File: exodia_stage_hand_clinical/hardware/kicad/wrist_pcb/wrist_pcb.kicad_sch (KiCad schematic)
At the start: 9 parts, among them Q1 IRLZ44N, Q2 2N7002, Q3 2N7002, Q4 2N7002, Q5 2N7002, U1 ESP32S3_MODULE, U2 TP4056_IC

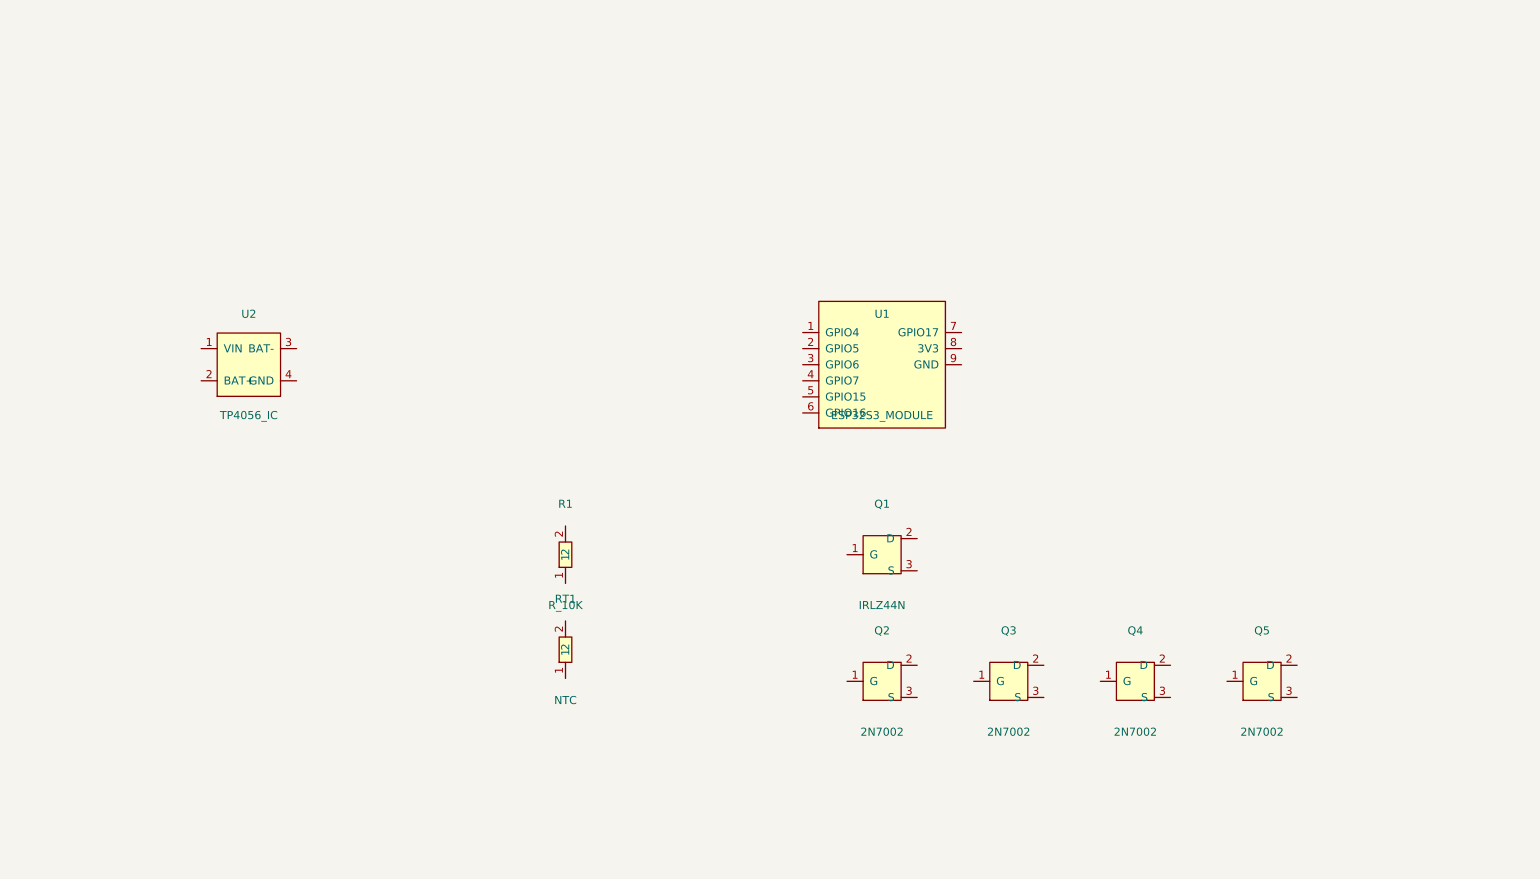
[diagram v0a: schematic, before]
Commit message: Auto-wire components using KiCad local labels and add ZIF/USB connectors
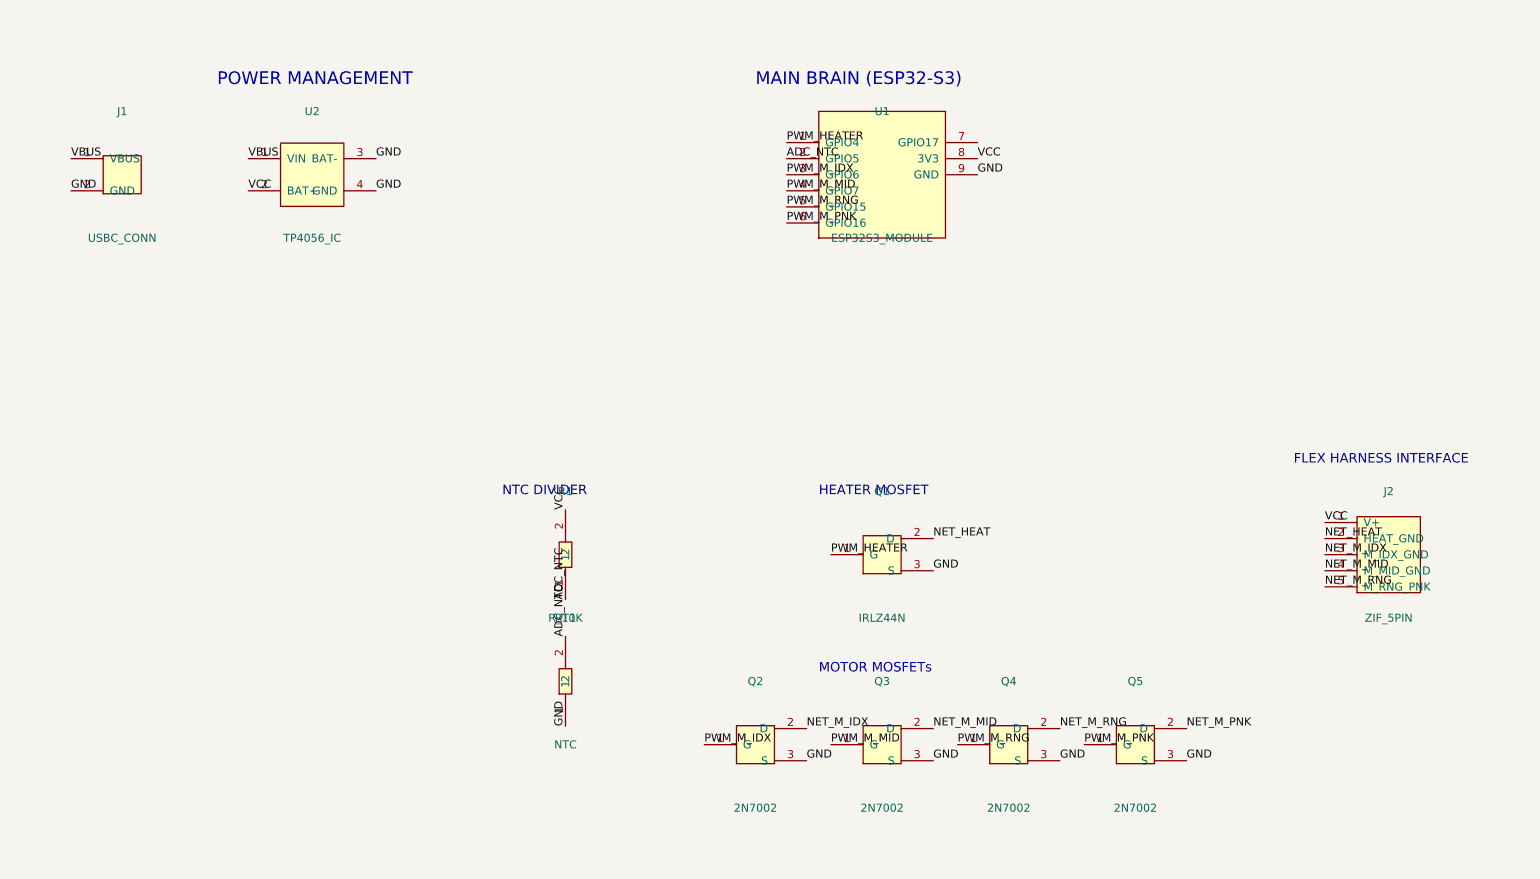
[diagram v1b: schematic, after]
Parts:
- added J1: USBC_CONN, symbol USBC_CONN
- added J2: ZIF_5PIN, symbol ZIF_5PIN
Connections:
- net VBUS: now reaches U2.1 (VIN)
- net VBUS: now also J1.1 (VBUS)
- net VCC: now reaches U2.2 (BAT+)
- net VCC: now also R1.2, U1.8 (3V3), J2.1 (V+)
- net GND: now reaches U2.3 (BAT-)
- net GND: now also Q1.3 (S), Q2.3 (S), Q3.3 (S), Q4.3 (S), Q5.3 (S), RT1.1, U1.9 (GND), U2.4 (GND), J1.2 (GND)
- net PWM_M_MID: now reaches Q3.1 (G)
- net PWM_M_MID: now also U1.4 (GPIO7)
- net NET_M_MID: now reaches Q3.2 (D)
- net NET_M_MID: now also J2.4 (M_MID_GND)
- net PWM_HEATER: now reaches Q1.1 (G)
- net PWM_HEATER: now also U1.1 (GPIO4)
- net NET_HEAT: now reaches Q1.2 (D)
- net NET_HEAT: now also J2.2 (HEAT_GND)
- net ADC_NTC: now reaches RT1.2
- net ADC_NTC: now also R1.1, U1.2 (GPIO5)
- net PWM_M_RNG: now reaches Q4.1 (G)
- net PWM_M_RNG: now also U1.5 (GPIO15)
- net NET_M_RNG: now reaches Q4.2 (D)
- net NET_M_RNG: now also J2.5 (M_RNG_PNK)
- net PWM_M_IDX: now reaches Q2.1 (G)
- net PWM_M_IDX: now also U1.3 (GPIO6)
- net NET_M_IDX: now reaches Q2.2 (D)
- net NET_M_IDX: now also J2.3 (M_IDX_GND)
- net PWM_M_PNK: now reaches Q5.1 (G)
- net PWM_M_PNK: now also U1.6 (GPIO16)
- net NET_M_PNK: now reaches Q5.2 (D)
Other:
- note added: "FLEX HARNESS INTERFACE"
- note added: "HEATER MOSFET"
- note added: "MAIN BRAIN (ESP32-S3)"
- note added: "MOTOR MOSFETs"
- note added: "NTC DIVIDER"
- note added: "POWER MANAGEMENT"

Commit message: Fix KiCad ERC errors (power flags, grid alignment, pin direction)
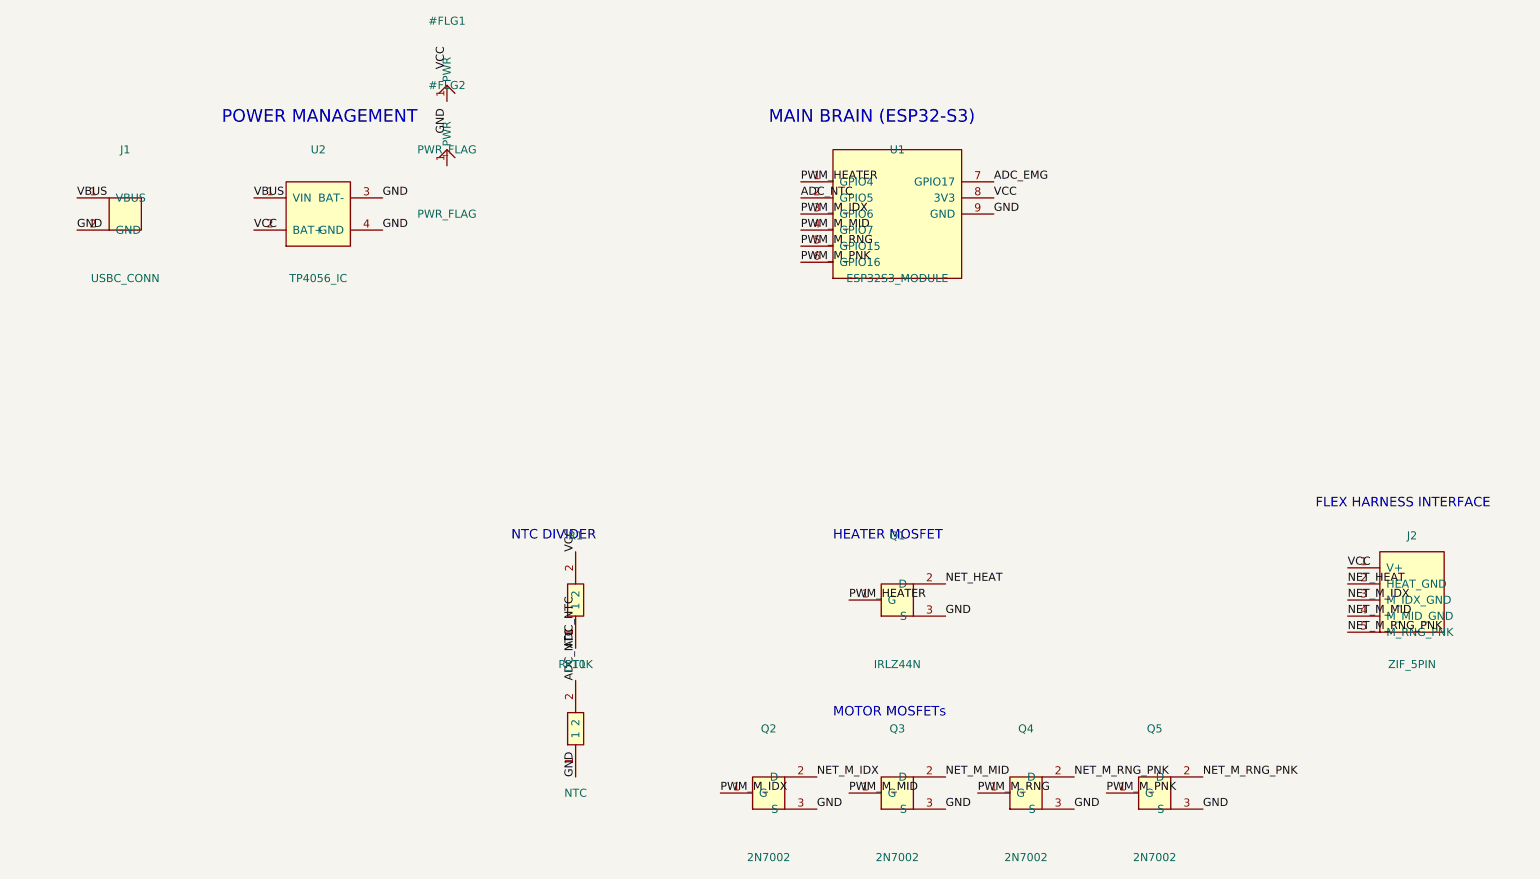
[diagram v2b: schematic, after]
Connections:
- net NET_M_RNG is gone; now on net NET_M_RNG_PNK: J2.5 (M_RNG_PNK), Q4.2 (D)
- net ADC_EMG: now reaches U1.7 (GPIO17)
- net NET_M_PNK renamed NET_M_RNG_PNK

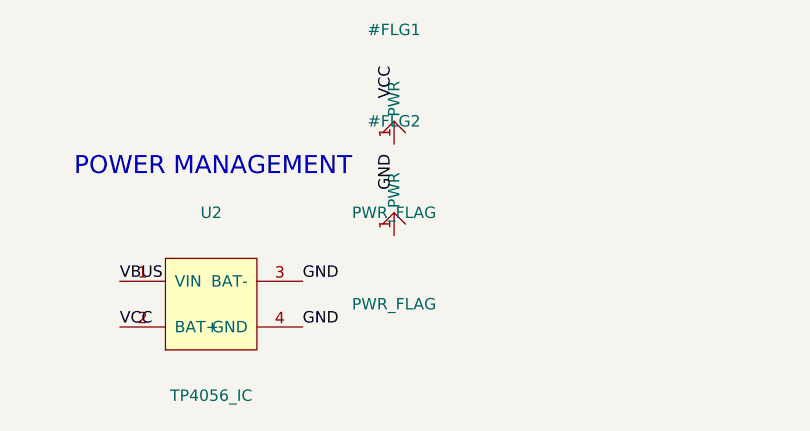
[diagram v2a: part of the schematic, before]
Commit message: Fix final KiCad ERC issues with power conflicts and label positioning
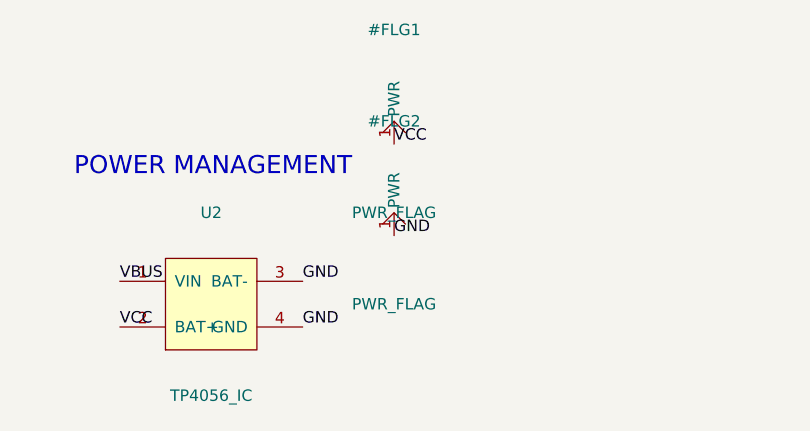
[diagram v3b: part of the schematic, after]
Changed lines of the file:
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@@
     (title "Exodia Stage Hand - Clinical Wrist PCB")
     (date "2026-05-15")
-    (rev "v1.1")
+    (rev "v1.2")
     (company "Resonanx")
   )
@@
   (label "NET_M_MID" (at 223.52 139.7 180) (effects (font (size 1.27 1.27)) (justify left bottom)))
   (label "NET_M_RNG_PNK" (at 223.52 142.24 180) (effects (font (size 1.27 1.27)) (justify left bottom)))
-  (label "VCC" (at 81.28 53.34 90) (effects (font (size 1.27 1.27)) (justify left bottom)))
-  (label "GND" (at 81.28 63.50000000000001 90) (effects (font (size 1.27 1.27)) (justify left bottom)))
+  (label "VCC" (at 81.28 58.42 0) (effects (font (size 1.27 1.27)) (justify left bottom)))
+  (label "GND" (at 81.28 68.58000000000001 0) (effects (font (size 1.27 1.27)) (justify left bottom)))
 )

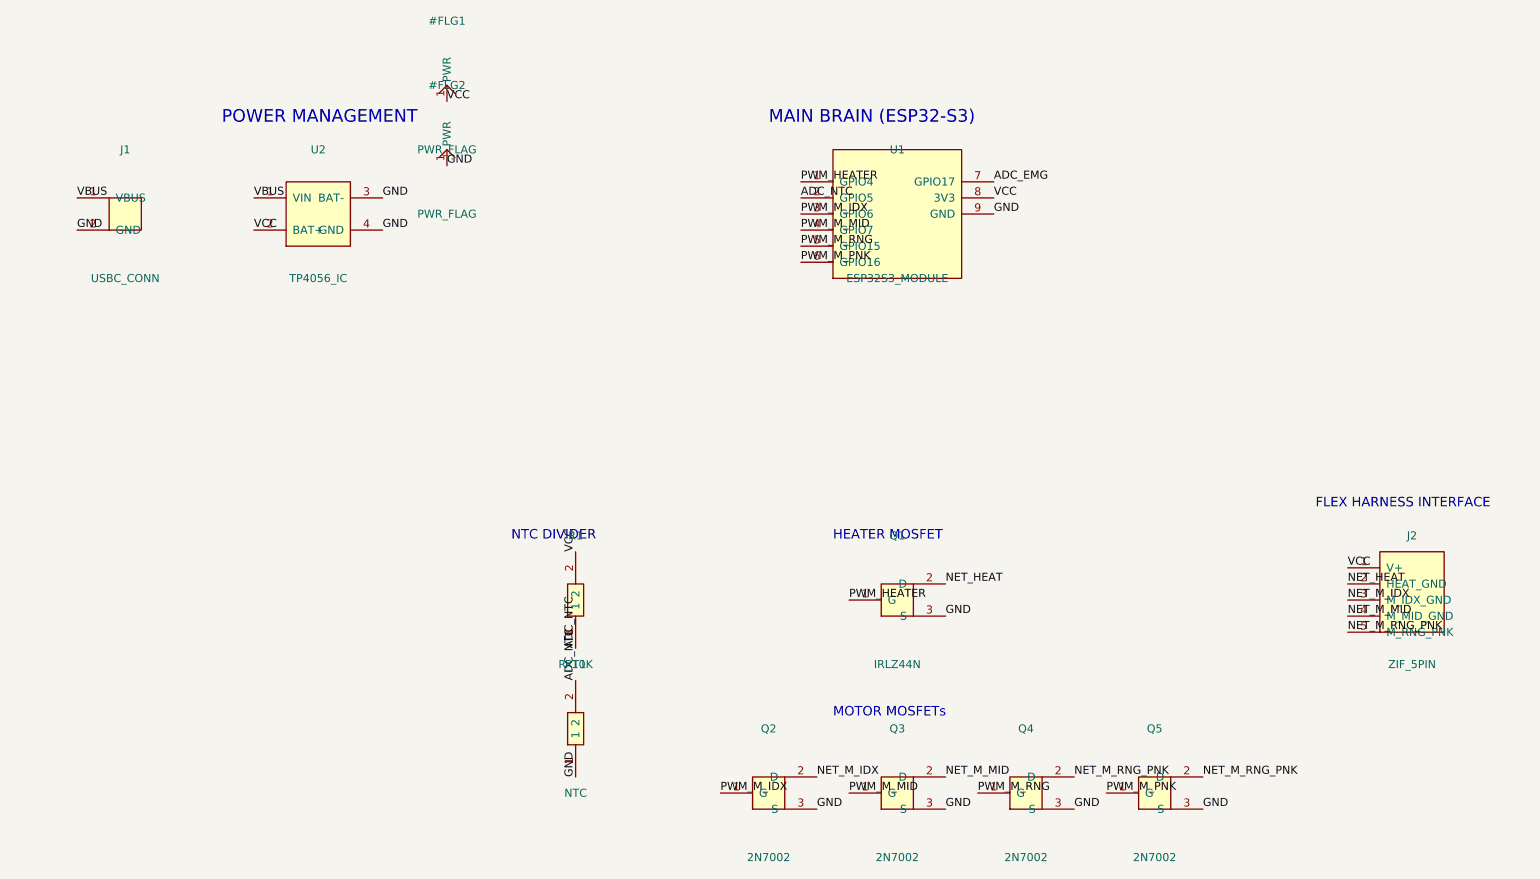
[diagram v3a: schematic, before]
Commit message: Fix footprint mapping errors by using exact physical pad numbering
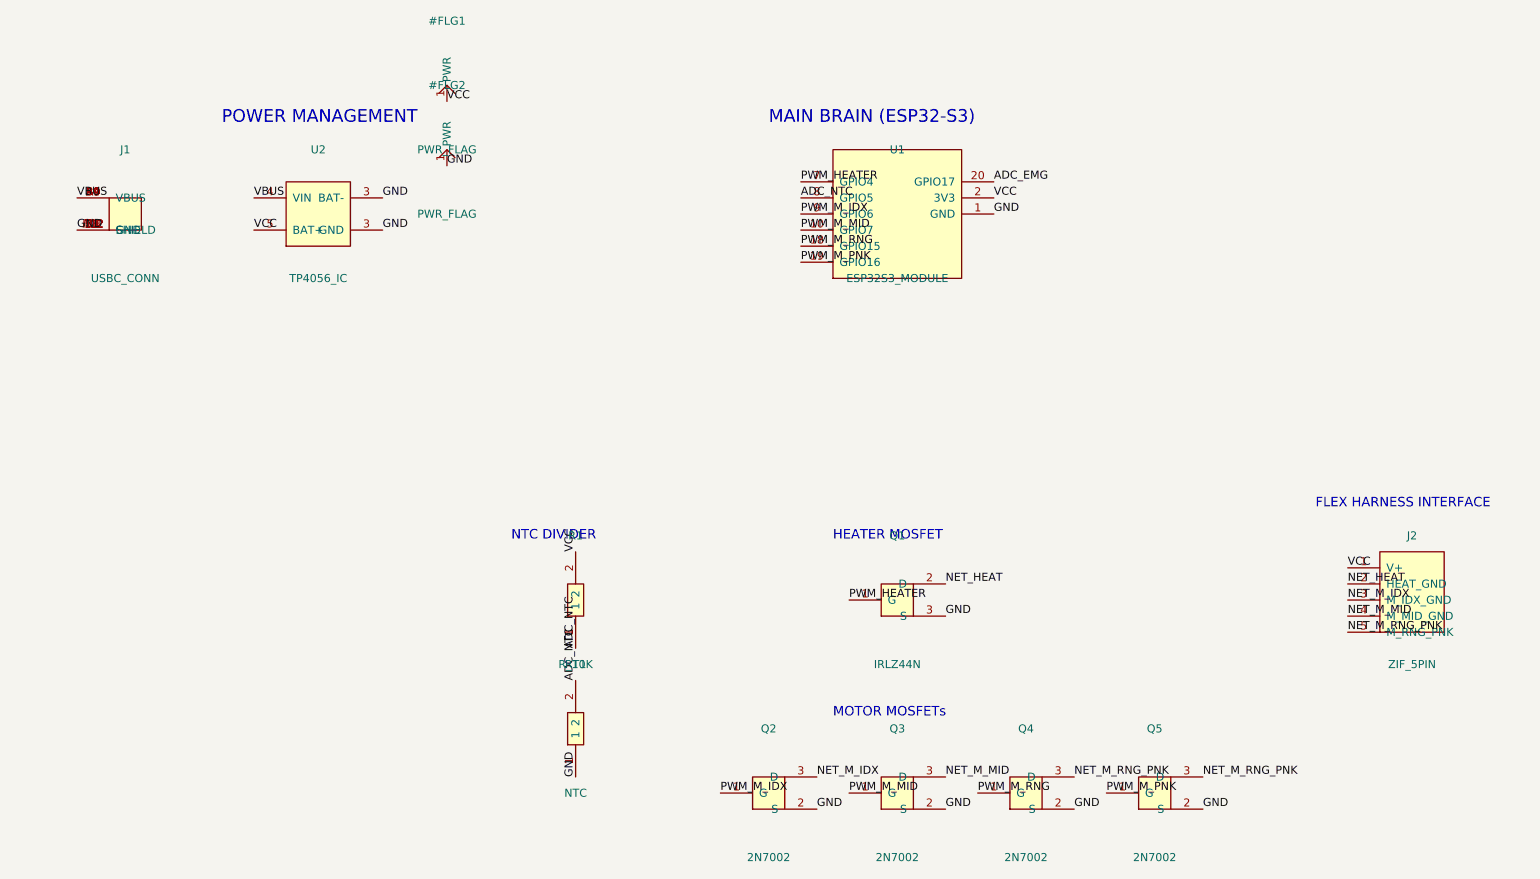
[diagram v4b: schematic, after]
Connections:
- net ADC_EMG: now also U1.20 (GPIO17); no longer U1.7 (GPIO17)
- net ADC_NTC: now also U1.8 (GPIO5); no longer U1.2 (GPIO5)
- net GND: now also J1.A1 (GND), J1.A12 (GND), J1.B1 (GND), J1.B12 (GND), J1.SH (SHIELD), Q2.2 (S), Q3.2 (S), Q4.2 (S), Q5.2 (S), U1.1 (GND); no longer J1.2 (GND), Q2.3 (S), Q3.3 (S), Q4.3 (S), Q5.3 (S), U1.9 (GND), U2.4 (GND)
- net NET_M_IDX: now also Q2.3 (D); no longer Q2.2 (D)
- net NET_M_MID: now also Q3.3 (D); no longer Q3.2 (D)
- net NET_M_RNG_PNK: now also Q4.3 (D), Q5.3 (D); no longer Q4.2 (D), Q5.2 (D)
- net PWM_HEATER: now also U1.7 (GPIO4); no longer U1.1 (GPIO4)
- net PWM_M_IDX: now also U1.9 (GPIO6); no longer U1.3 (GPIO6)
- net PWM_M_MID: now also U1.10 (GPIO7); no longer U1.4 (GPIO7)
- net PWM_M_PNK: now also U1.19 (GPIO16); no longer U1.6 (GPIO16)
- net PWM_M_RNG: now also U1.18 (GPIO15); no longer U1.5 (GPIO15)
- net VBUS: now also J1.A4 (VBUS), J1.A9 (VBUS), J1.B4 (VBUS), J1.B9 (VBUS), U2.4 (VIN); no longer J1.1 (VBUS), U2.1 (VIN)
- net VCC: now also U1.2 (3V3), U2.5 (BAT+); no longer U1.8 (3V3), U2.2 (BAT+)
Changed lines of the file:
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@@
     (title "Exodia Stage Hand - Clinical Wrist PCB")
     (date "2026-05-15")
-    (rev "v1.2")
+    (rev "v1.3")
     (company "Resonanx")
   )
